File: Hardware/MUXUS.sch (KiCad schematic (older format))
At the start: 122 parts, among them J1 USB_C_Receptacle_USB2.0, J10 VCP, J2 USB_B, J3 USB_A, J4 USB_B, J5 USB_A, J6 STDC14, J7 USB_B, J8 USB_A, J9 SWD, SW1 USER, SW2 RESET, U1 USBLC6-4SC6, U10 AP2151W, U11 AOZ1212AI, U12 USBLC6-2SC6, U13 USBLC6-2SC6, U14 AP2151W, U2 USB2504A-JT, U3 USBLC6-2SC6, U4 USBLC6-2SC6, U5 AP2151W, U6 TS3USBCA420RSVR, U7 STM32G431K8T6, U8 USBLC6-2SC6, U9 USBLC6-2SC6, Y1 ATS240C

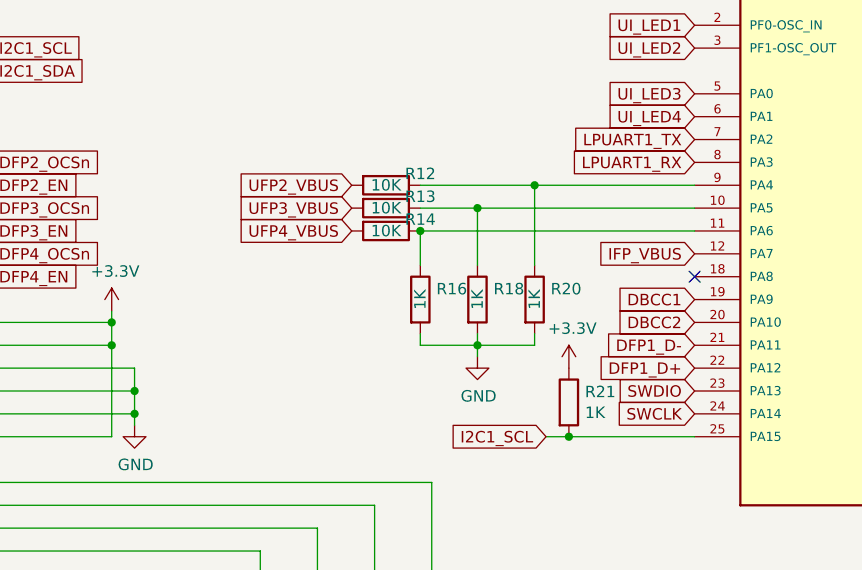
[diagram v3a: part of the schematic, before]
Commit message: Measure UFP1_VBUS as well for the UCPD stack
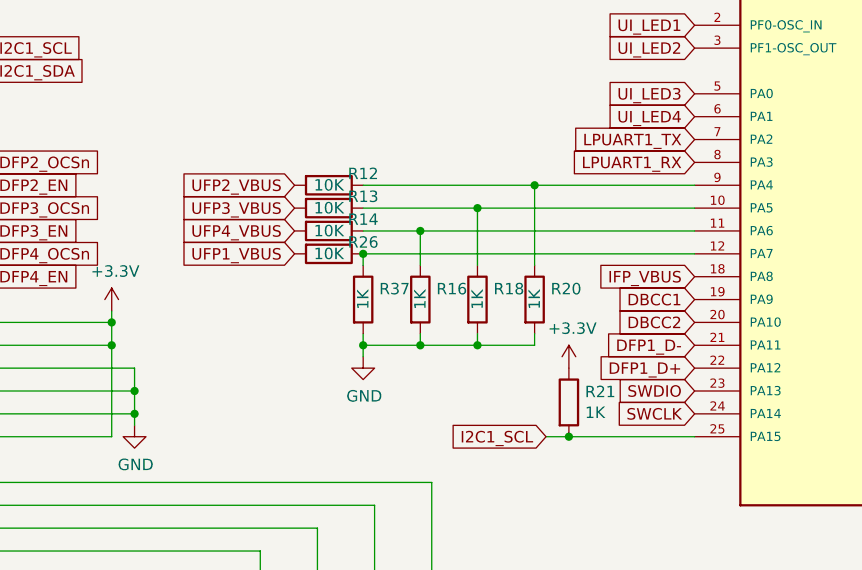
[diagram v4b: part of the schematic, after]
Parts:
- added R26: 10K, Resistor_SMD:R_1206_3216Metric, symbol Device:R
- added R37: 1K, Resistor_SMD:R_1206_3216Metric, symbol Device:R
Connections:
- net GND: now also R37.2
- net IFP_VBUS: now also U7.18 (PA8); no longer U7.12 (PA7)
- net VBUS: now also R26.2
- new net: R26.1, R37.1, U7.12 (PA7)
- no-connect marks 10 -> 9
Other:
- moved on the sheet: R12, R13, R14
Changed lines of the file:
@@
 Text GLabel 1700 6950 0    50   Input ~ 0
 IFP_VBUS
-Text GLabel 7300 6900 0    50   Input ~ 0
+Text GLabel 7300 7000 0    50   Input ~ 0
 IFP_VBUS
 Text GLabel 8900 6500 2    50   Input ~ 0
@@
 	-1   0    0    1
 $EndComp
-Wire Wire Line
-	7300 6600 6600 6600
 $Comp
 L Device:R R14
 U 1 1 6241BDE6
-P 5950 6800
-F 0 "R14" V 5900 6950 50  0000 C CNN
-F 1 "10K" V 5950 6800 50  0000 C CNN
-F 2 "Resistor_SMD:R_1206_3216Metric" V 5880 6800 50  0001 C CNN
-F 3 "~" H 5950 6800 50  0001 C CNN
-	1    5950 6800
+P 5700 6800
+F 0 "R14" V 5650 6950 50  0000 C CNN
+F 1 "10K" V 5700 6800 50  0000 C CNN
+F 2 "Resistor_SMD:R_1206_3216Metric" V 5630 6800 50  0001 C CNN
+F 3 "~" H 5700 6800 50  0001 C CNN
+	1    5700 6800
 	0    1    1    0
 $EndComp
@@
 L Device:R R13
 U 1 1 6241B806
-P 5950 6700
-F 0 "R13" V 5900 6850 50  0000 C CNN
-F 1 "10K" V 5950 6700 50  0000 C CNN
-F 2 "Resistor_SMD:R_1206_3216Metric" V 5880 6700 50  0001 C CNN
-F 3 "~" H 5950 6700 50  0001 C CNN
-	1    5950 6700
+P 5700 6700
+F 0 "R13" V 5650 6850 50  0000 C CNN
+F 1 "10K" V 5700 6700 50  0000 C CNN
+F 2 "Resistor_SMD:R_1206_3216Metric" V 5630 6700 50  0001 C CNN
+F 3 "~" H 5700 6700 50  0001 C CNN
+	1    5700 6700
 	0    1    1    0
 $EndComp
@@
 L Device:R R12
 U 1 1 62418C95
-P 5950 6600
-F 0 "R12" V 5900 6750 50  0000 C CNN
-F 1 "10K" V 5950 6600 50  0000 C CNN
-F 2 "Resistor_SMD:R_1206_3216Metric" V 5880 6600 50  0001 C CNN
-F 3 "~" H 5950 6600 50  0001 C CNN
-	1    5950 6600
-	0    1    1    0
-$EndComp
-Text GLabel 5800 6800 0    50   Input ~ 0
+P 5700 6600
+F 0 "R12" V 5650 6750 50  0000 C CNN
+F 1 "10K" V 5700 6600 50  0000 C CNN
+F 2 "Resistor_SMD:R_1206_3216Metric" V 5630 6600 50  0001 C CNN
+F 3 "~" H 5700 6600 50  0001 C CNN
+	1    5700 6600
+	0    1    1    0
+$EndComp
+Text GLabel 5550 6800 0    50   Input ~ 0
 UFP4_VBUS
-Text GLabel 5800 6700 0    50   Input ~ 0
+Text GLabel 5550 6700 0    50   Input ~ 0
 UFP3_VBUS
-Text GLabel 5800 6600 0    50   Input ~ 0
+Text GLabel 5550 6600 0    50   Input ~ 0
 UFP2_VBUS
 $Comp
@@
 $EndComp
 Wire Wire Line
-	6100 6950 6100 6800
-Wire Wire Line
-	6350 6950 6350 6700
-Wire Wire Line
-	6350 6700 7300 6700
-Wire Wire Line
-	6600 6950 6600 6600
-Connection ~ 6600 6600
-Wire Wire Line
-	6600 6600 6100 6600
-Wire Wire Line
-	6100 6800 7300 6800
-Connection ~ 6100 6800
-Wire Wire Line
-	6100 6700 6350 6700
-Connection ~ 6350 6700
+	5850 6800 6100 6800
 $Comp
 L power:GND #PWR015
 U 1 1 6260B042
-P 6350 7350
-F 0 "#PWR015" H 6350 7100 50  0001 C CNN
-F 1 "GND" H 6355 7177 50  0000 C CNN
-F 2 "" H 6350 7350 50  0001 C CNN
-F 3 "" H 6350 7350 50  0001 C CNN
-	1    6350 7350
-	1    0    0    -1
-$EndComp
-Wire Wire Line
-	6350 7350 6350 7300
+P 5850 7350
+F 0 "#PWR015" H 5850 7100 50  0001 C CNN
+F 1 "GND" H 5855 7177 50  0000 C CNN
+F 2 "" H 5850 7350 50  0001 C CNN
+F 3 "" H 5850 7350 50  0001 C CNN
+	1    5850 7350
+	1    0    0    -1
+$EndComp
 Wire Wire Line
 	6350 7300 6100 7300
@@
 	10400 9450 10400 9350
 Connection ~ 10400 9450
-NoConn ~ 7300 7000
 Connection ~ 6750 7700
 Wire Wire Line
@@
 Text GLabel 12250 9050 0    50   Input ~ 0
 LPUART1_RX
+Wire Wire Line
+	5850 6600 6600 6600
+Wire Wire Line
+	5850 6700 6350 6700
+$Comp
+L Device:R R26
+U 1 1 615C410A
+P 5700 6900
+F 0 "R26" V 5650 7050 50  0000 C CNN
+F 1 "10K" V 5700 6900 50  0000 C CNN
+F 2 "Resistor_SMD:R_1206_3216Metric" V 5630 6900 50  0001 C CNN
+F 3 "~" H 5700 6900 50  0001 C CNN
+	1    5700 6900
+	0    1    1    0
+$EndComp
+Wire Wire Line
+	7300 6900 5850 6900
+$Comp
+L Device:R R37
+U 1 1 6167BF5A
+P 5850 7100
+F 0 "R37" H 5920 7146 50  0000 L CNN
+F 1 "1K" V 5850 7100 50  0000 C CNN
+F 2 "Resistor_SMD:R_1206_3216Metric" V 5780 7100 50  0001 C CNN
+F 3 "~" H 5850 7100 50  0001 C CNN
+	1    5850 7100
+	1    0    0    -1
+$EndComp
+Connection ~ 6100 7300
+Wire Wire Line
+	5850 7300 5850 7250
+Wire Wire Line
+	5850 7300 6100 7300
+Wire Wire Line
+	5850 7350 5850 7300
+Connection ~ 5850 7300
+Wire Wire Line
+	5850 6950 5850 6900
+Connection ~ 5850 6900
+Wire Wire Line
+	6100 6950 6100 6800
+Connection ~ 6100 6800
+Wire Wire Line
+	6100 6800 7300 6800
+Wire Wire Line
+	6350 6950 6350 6700
+Connection ~ 6350 6700
+Wire Wire Line
+	6350 6700 7300 6700
+Wire Wire Line
+	6600 6950 6600 6600
+Connection ~ 6600 6600
+Wire Wire Line
+	6600 6600 7300 6600
+Text GLabel 5550 6900 0    50   Input ~ 0
+UFP1_VBUS
 $EndSCHEMATC
